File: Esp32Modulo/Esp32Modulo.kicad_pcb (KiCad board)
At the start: 2 copper layers, 50 x 50 mm, 22 parts, among them J4 Alimentacion, U1 ESP32, U2 AMS1117-3.3

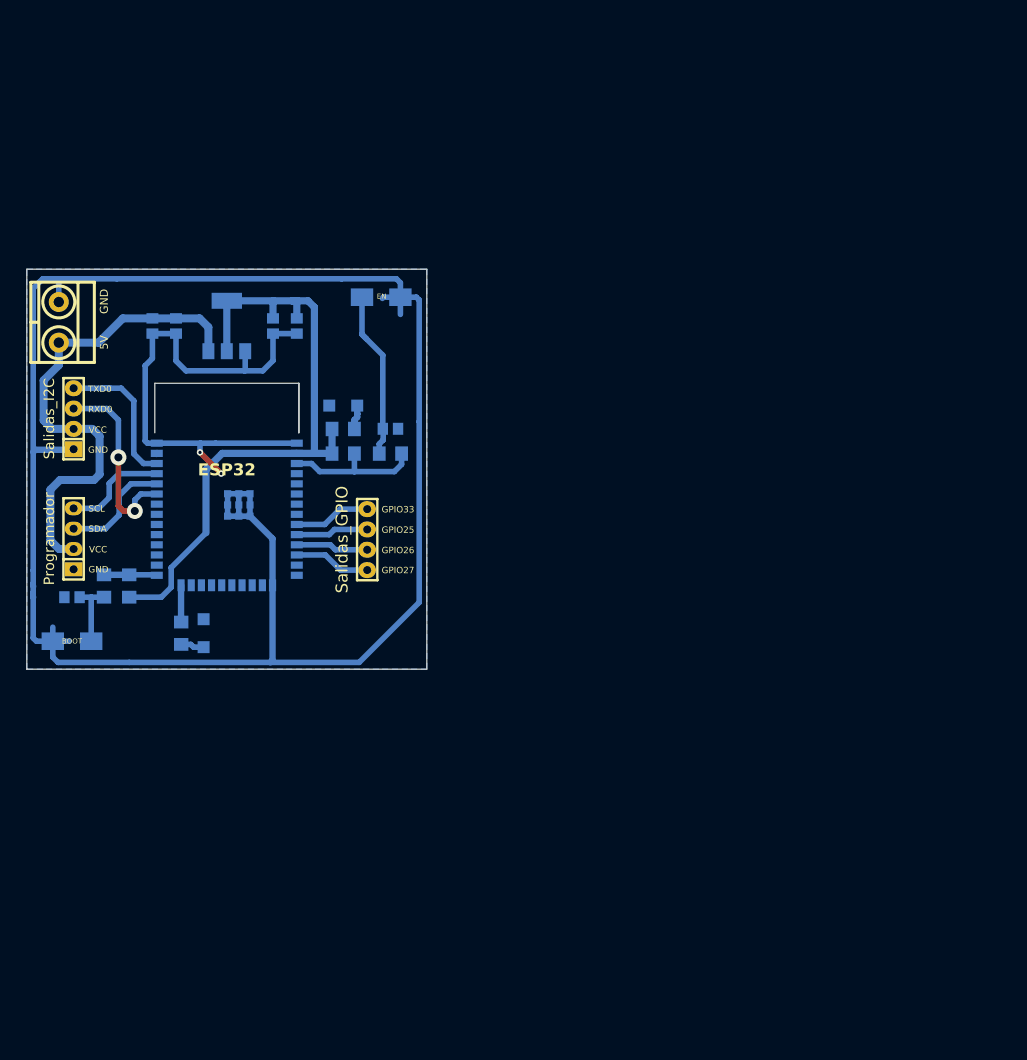
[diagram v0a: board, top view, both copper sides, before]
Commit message: modificaciones al PCB para arreglar el error de pasar pistas por encima de la antena
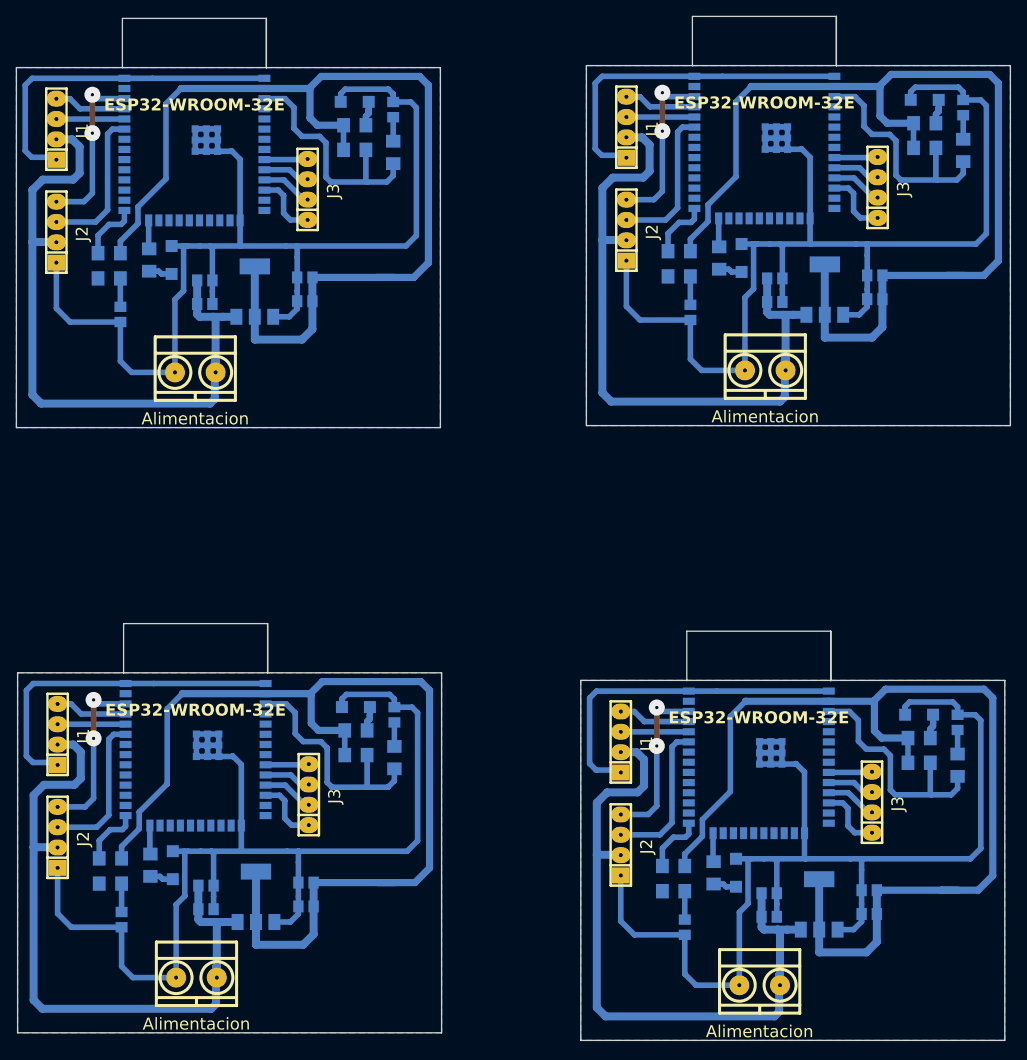
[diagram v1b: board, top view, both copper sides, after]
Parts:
- removed BOOT, EN: SW_Push, footprints:Button
- removed the J4 at (102.2, 71.9)
- removed Programador: Programador, EESTN5:pin_strip_4
- removed Salidas_GPIO: Salidas_GPIO, EESTN5:pin_strip_4
- removed Salidas_I2C: Salidas_I2C(5V), EESTN5:pin_strip_4
- added C1: 10uF, EESTN5:C_0805, B.Cu at (120.6, 145.3)
- added C1: 10uF, EESTN5:C_0805, B.Cu at (191.0, 146.2)
- added C1: 10uF, EESTN5:C_0805, B.Cu at (191.7, 69.4)
- added C2: 100nF, EESTN5:C_0805, B.Cu at (120.6, 142.3)
- added C2: 100nF, EESTN5:C_0805, B.Cu at (191.0, 143.3)
- added C2: 100nF, EESTN5:C_0805, B.Cu at (191.7, 66.5)
- added C3: 10uF, EESTN5:C_0805, B.Cu at (133.2, 142.0)
- added C3: 10uF, EESTN5:C_0805, B.Cu at (204.3, 66.1)
- added C3: 10uF, EESTN5:C_0805, B.Cu at (203.6, 142.9)
- added C4: 100nF, EESTN5:C_0805, B.Cu at (203.6, 145.9)
- added C4: 100nF, EESTN5:C_0805, B.Cu at (204.3, 69.0)
- added C4: 100nF, EESTN5:C_0805, B.Cu at (133.2, 144.9)
- added C5: 1n, EESTN5:C_0805, B.Cu at (181.2, 70.7)
- added C5: 1n, EESTN5:C_0805, B.Cu at (180.5, 147.6)
- added C5: 1n, EESTN5:C_0805, B.Cu at (110.1, 146.6)
- added C6: 1n, EESTN5:C_0805, B.Cu at (215.3, 45.1)
- added C6: 1n, EESTN5:C_0805, B.Cu at (214.6, 122.0)
- added C6: 1n, EESTN5:C_0805, B.Cu at (144.2, 121.0)
- added J1: Programador, EESTN5:pin_strip_4, F.Cu at (102.0, 47.8)
- added J1: Programador, EESTN5:pin_strip_4, F.Cu at (173.2, 47.5)
- added J1: Programador, EESTN5:pin_strip_4, F.Cu at (102.1, 123.5)
- added J1: Programador, EESTN5:pin_strip_4, F.Cu at (172.5, 124.4)
- added J2: Salidas_I2C(5V), EESTN5:pin_strip_4, F.Cu at (102.0, 60.7)
- added J2: Salidas_I2C(5V), EESTN5:pin_strip_4, F.Cu at (102.1, 136.3)
- added J2: Salidas_I2C(5V), EESTN5:pin_strip_4, F.Cu at (172.5, 137.3)
- added J2: Salidas_I2C(5V), EESTN5:pin_strip_4, F.Cu at (173.2, 60.4)
- added J3: Salidas_GPIO, EESTN5:pin_strip_4, F.Cu at (133.5, 131.0)
- added J3: Salidas_GPIO, EESTN5:pin_strip_4, F.Cu at (203.9, 131.9)
- added J3: Salidas_GPIO, EESTN5:pin_strip_4, F.Cu at (204.6, 55.1)
- added J3: Salidas_GPIO, EESTN5:pin_strip_4, F.Cu at (133.3, 55.3)
- added J4: Alimentacion, EESTN5:BORNERA2_AZUL, F.Cu at (189.9, 154.8)
- added J4: Alimentacion, EESTN5:BORNERA2_AZUL, F.Cu at (119.5, 153.8)
- added J4: Alimentacion, EESTN5:BORNERA2_AZUL, F.Cu at (190.6, 78.0)
- added J4: Alimentacion, EESTN5:BORNERA2_AZUL, F.Cu at (119.3, 78.2)
- added LED1: POW, EESTN5:LED_1206, B.Cu at (139.4, 120.0)
- added LED1: POW, EESTN5:LED_1206, B.Cu at (210.5, 44.1)
- added LED1: POW, EESTN5:LED_1206, B.Cu at (209.8, 121.0)
- added LED2: D2, EESTN5:LED_1206, B.Cu at (186.9, 140.7)
- added LED2: D2, EESTN5:LED_1206, B.Cu at (187.6, 63.9)
- added LED2: D2, EESTN5:LED_1206, B.Cu at (116.5, 139.8)
- added R1: 470, EESTN5:R_1206, B.Cu at (108.7, 142.1)
- added R1: 470, EESTN5:R_1206, B.Cu at (179.8, 66.2)
- added R1: 470, EESTN5:R_1206, B.Cu at (179.1, 143.1)
- added R3: 1OK, EESTN5:R_1206, B.Cu at (108.7, 138.9)
- added R3: 1OK, EESTN5:R_1206, B.Cu at (179.8, 63.0)
- added R3: 1OK, EESTN5:R_1206, B.Cu at (179.1, 139.9)
- added R5: 1K, EESTN5:R_1206, B.Cu at (139.4, 123.0)
- added R5: 1K, EESTN5:R_1206, B.Cu at (209.8, 123.9)
- added R5: 1K, EESTN5:R_1206, B.Cu at (210.5, 47.1)
- added R6: 1K, EESTN5:R_1206, B.Cu at (184.8, 63.9)
- added R6: 1K, EESTN5:R_1206, B.Cu at (113.7, 139.8)
- added R6: 1K, EESTN5:R_1206, B.Cu at (184.1, 140.8)
- added R7: 470, EESTN5:R_1206, B.Cu at (214.6, 127.3)
- added R7: 470, EESTN5:R_1206, B.Cu at (215.3, 50.5)
- added R7: 470, EESTN5:R_1206, B.Cu at (144.2, 126.4)
- added R8: 10K, EESTN5:R_1206, B.Cu at (210.5, 50.1)
- added R8: 10K, EESTN5:R_1206, B.Cu at (209.8, 127.0)
- added R8: 10K, EESTN5:R_1206, B.Cu at (139.4, 126.0)
- added U1: ESP32-WROOM-32E, footprints:ESP32-WROOM-32E, B.Cu at (189.8, 126.3)
- added U1: ESP32-WROOM-32E, footprints:ESP32-WROOM-32E, B.Cu at (190.4, 49.4)
- added U1: ESP32-WROOM-32E, footprints:ESP32-WROOM-32E, B.Cu at (119.3, 125.3)
- added U2: AMS1117-3.3, footprints:SOT-223-3_TabPin2, B.Cu at (126.9, 143.8)
- added U2: AMS1117-3.3, footprints:SOT-223-3_TabPin2, B.Cu at (197.3, 144.7)
- added U2: AMS1117-3.3, footprints:SOT-223-3_TabPin2, B.Cu at (198.0, 67.8)
- U1: value ESP32 -> ESP32-WROOM-32E
- moved LED2 46.8 mm to (116.3, 64.1)
- moved R6 46.8 mm to (113.5, 64.2)
- moved U1 45.8 mm to (119.2, 49.7)
- moved R3 41.7 mm to (108.5, 63.3), turned to 180 degrees
- moved C6 39.9 mm to (144.1, 45.4), turned to 90 degrees
- moved R1 38.5 mm to (108.5, 66.5), turned to 0 degrees
- moved R5 38.0 mm to (139.2, 47.3)
- moved LED1 38.0 mm to (139.2, 44.4)
- moved R8 38.0 mm to (139.2, 50.4)
- moved R7 37.6 mm to (144.1, 50.7), turned to 90 degrees
- moved C5 35.9 mm to (110.0, 71.0), turned to -90 degrees
- moved C3 7.26 mm to (133.0, 66.3), turned to 0 degrees
- moved C1 7.10 mm to (120.5, 69.7), turned to 180 degrees
- moved C2 6.74 mm to (120.5, 66.7), turned to 180 degrees
- moved U2 5.54 mm to (126.8, 68.1)
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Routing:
- net GND: track 303.5 -> 778.8 mm, vias 2 -> 0
- net +3V3: track 83.0 -> 520.1 mm
- net +5V: track 63.1 -> 346.3 mm
- net /EN: track 17.5 -> 121.4 mm
- net /SCL: track 19.3 -> 85.8 mm, vias 0 -> 8
- net /SDA: track 23.9 -> 75.5 mm, vias 2 -> 0
- net /IO0: track 6.62 -> 30.4 mm
- net /IO27: track 9.58 -> 33.0 mm
- net /TXD0: track 13.2 -> 36.1 mm
- net /RXD0: track 14.1 -> 34.0 mm
- net /IO26: track 9.06 -> 25.7 mm
- net /IO25: track 9.07 -> 23.6 mm
- net /IO33: track 9.60 -> 21.7 mm
- net Net-(LED1-A): track 3.44 -> 13.7 mm
- net /IO2: track 4.62 -> 14.3 mm
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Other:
- board size 50 x 50 mm -> 124.2 x 121.8 mm
- board text removed: "5V"
- board text removed: "GND"
- board text removed: "GPIO25"
- board text removed: "GPIO26"
- board text removed: "GPIO27"
- board text removed: "GPIO33"
- board text removed: "RXD0"
- board text removed: "SCL"
- board text removed: "SDA"
- board text removed: "TXD0"
- board text removed: "VCC"

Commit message: PCB con el error de la antena corregido y terminado
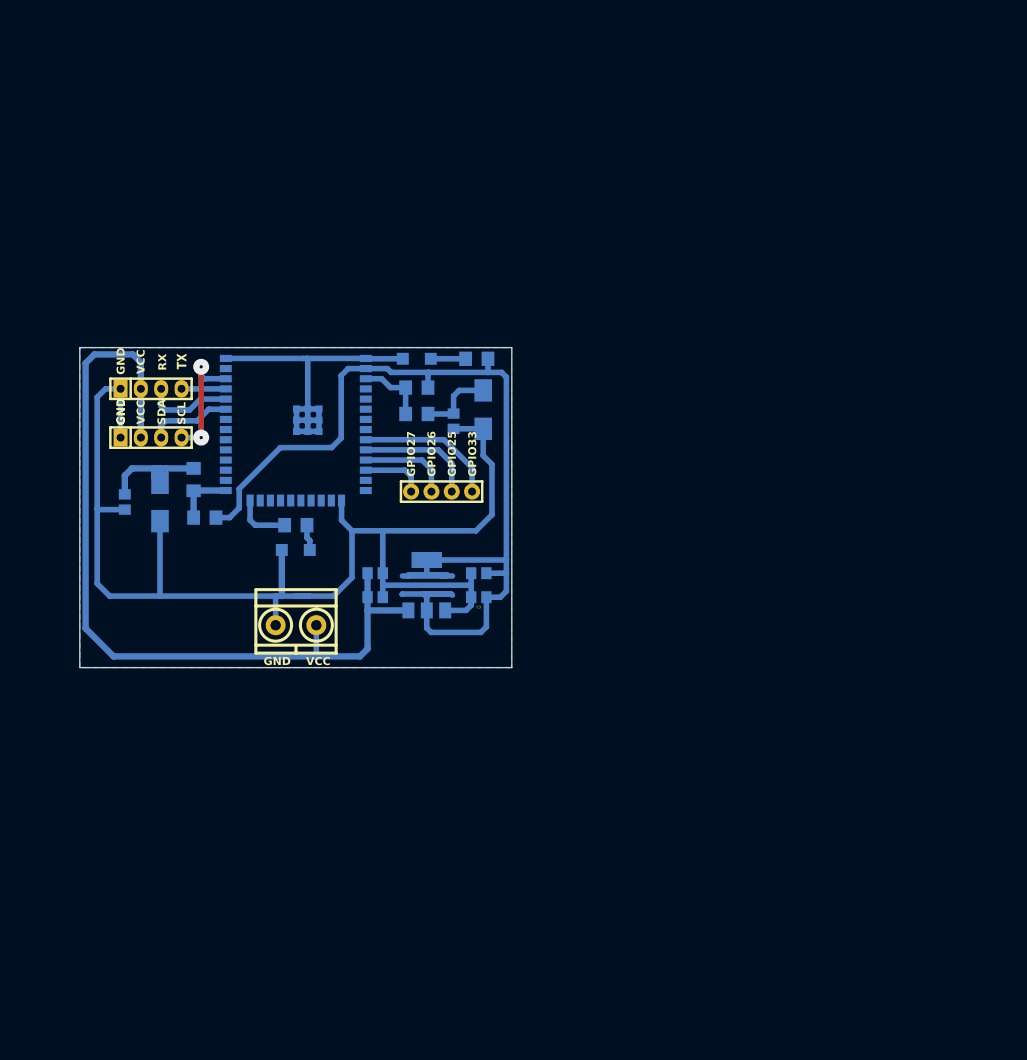
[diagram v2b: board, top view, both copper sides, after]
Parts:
- removed the C1 at (120.6, 145.3)
- removed the C1 at (191.0, 146.2)
- removed the C1 at (191.7, 69.4)
- removed the C1 at (120.5, 69.7)
- removed the C2 at (120.6, 142.3)
- removed the C2 at (191.0, 143.3)
- removed the C2 at (191.7, 66.5)
- removed the C2 at (120.5, 66.7)
- removed the C3 at (133.2, 142.0)
- removed the C3 at (204.3, 66.1)
- removed the C3 at (133.0, 66.3)
- removed the C3 at (203.6, 142.9)
- removed the C4 at (133.0, 69.3)
- removed the C4 at (203.6, 145.9)
- removed the C4 at (204.3, 69.0)
- removed the C4 at (133.2, 144.9)
- removed the C5 at (181.2, 70.7)
- removed the C5 at (180.5, 147.6)
- removed the C5 at (110.0, 71.0)
- removed the C5 at (110.1, 146.6)
- removed the C6 at (215.3, 45.1)
- removed the C6 at (144.1, 45.4)
- removed the C6 at (214.6, 122.0)
- removed the C6 at (144.2, 121.0)
- removed the J1 at (102.0, 47.8)
- removed the J1 at (173.2, 47.5)
- removed the J1 at (102.1, 123.5)
- removed the J1 at (172.5, 124.4)
- removed the J2 at (102.0, 60.7)
- removed the J2 at (102.1, 136.3)
- removed the J2 at (172.5, 137.3)
- removed the J2 at (173.2, 60.4)
- removed the J3 at (133.5, 131.0)
- removed the J3 at (203.9, 131.9)
- removed the J3 at (204.6, 55.1)
- removed the J3 at (133.3, 55.3)
- removed the J4 at (189.9, 154.8)
- removed the J4 at (119.5, 153.8)
- removed the J4 at (190.6, 78.0)
- removed the J4 at (119.3, 78.2)
- removed the LED1 at (139.4, 120.0)
- removed the LED1 at (210.5, 44.1)
- removed the LED1 at (139.2, 44.4)
- removed the LED1 at (209.8, 121.0)
- removed the LED2 at (186.9, 140.7)
- removed the LED2 at (116.3, 64.1)
- removed the LED2 at (187.6, 63.9)
- removed the LED2 at (116.5, 139.8)
- removed the R1 at (108.7, 142.1)
- removed the R1 at (108.5, 66.5)
- removed the R1 at (179.8, 66.2)
- removed the R1 at (179.1, 143.1)
- removed the R3 at (108.7, 138.9)
- removed the R3 at (179.8, 63.0)
- removed the R3 at (108.5, 63.3)
- removed the R3 at (179.1, 139.9)
- removed the R5 at (139.2, 47.3)
- removed the R5 at (139.4, 123.0)
- removed the R5 at (209.8, 123.9)
- removed the R5 at (210.5, 47.1)
- removed the R6 at (113.5, 64.2)
- removed the R6 at (184.8, 63.9)
- removed the R6 at (113.7, 139.8)
- removed the R6 at (184.1, 140.8)
- removed the R7 at (214.6, 127.3)
- removed the R7 at (215.3, 50.5)
- removed the R7 at (144.1, 50.7)
- removed the R7 at (144.2, 126.4)
- removed the R8 at (139.2, 50.4)
- removed the R8 at (210.5, 50.1)
- removed the R8 at (209.8, 127.0)
- removed the R8 at (139.4, 126.0)
- removed the U1 at (189.8, 126.3)
- removed the U1 at (190.4, 49.4)
- removed the U1 at (119.3, 125.3)
- removed the U1 at (119.2, 49.7)
- removed the U2 at (126.8, 68.1)
- removed the U2 at (126.9, 143.8)
- removed the U2 at (197.3, 144.7)
- removed the U2 at (198.0, 67.8)
- added BOOT1: SW_Push, footprints:Button, B.Cu at (114.9, 94.4)
- added C1: 10uF, EESTN5:C_0805, B.Cu at (141.8, 103.3)
- added C2: 100nF, EESTN5:C_0805, B.Cu at (141.8, 106.3)
- added C3: 10uF, EESTN5:C_0805, B.Cu at (154.7, 106.3)
- added C4: 100nF, EESTN5:C_0805, B.Cu at (154.7, 103.3)
- added C5: 1n, EESTN5:C_0805, B.Cu at (110.5, 94.4)
- added C6: 1n, EESTN5:C_0805, B.Cu at (151.6, 84.3)
- added EN1: SW_Push, footprints:Button, B.Cu at (155.3, 82.8)
- added J1: Programador, EESTN5:pin_strip_4, F.Cu at (113.8, 80.2)
- added J2: Salidas_I2C(5V), EESTN5:pin_strip_4, F.Cu at (113.8, 86.3)
- added J3: Salidas_GPIO, EESTN5:pin_strip_4, F.Cu at (150.1, 93.1)
- added J4: Alimentacion, EESTN5:BORNERA2_AZUL, F.Cu at (131.9, 109.8)
- added LED1: POW, EESTN5:LED_1206, B.Cu at (147.0, 76.5)
- added LED2: D2, EESTN5:LED_1206, B.Cu at (131.9, 100.4)
- added R1: 470, EESTN5:R_1206, B.Cu at (119.1, 91.6)
- added R3: 1OK, EESTN5:R_1206, B.Cu at (120.5, 96.3)
- added R5: 1K, EESTN5:R_1206, B.Cu at (154.5, 76.5)
- added R6: 1K, EESTN5:R_1206, B.Cu at (131.9, 97.3)
- added R7: 470, EESTN5:R_1206, B.Cu at (147.0, 83.4)
- added R8: 10K, EESTN5:R_1206, B.Cu at (147.0, 80.1)
- added U1: ESP32-WROOM-32E, footprints:ESP32-WROOM-32E, B.Cu at (131.9, 84.7)
- added U2: AMS1117-3.3, footprints:SOT-223-3_TabPin2, B.Cu at (148.2, 104.8)
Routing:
- net GND: track 778.8 -> 206.0 mm
- net +3V3: track 520.1 -> 135.2 mm
- net +5V: track 346.3 -> 105.9 mm
- net /EN: track 121.4 -> 8.74 mm
- net /SCL: track 85.8 -> 15.7 mm, vias 8 -> 2
- net /SDA: track 75.5 -> 10.5 mm
- net /TXD0: track 36.1 -> 5.54 mm
- net /IO27: track 33.0 -> 7.89 mm
- net /IO0: track 30.4 -> 7.39 mm
- net /RXD0: track 34.0 -> 11.0 mm
- net /IO26: track 25.7 -> 11.5 mm
- net Net-(LED1-A): track 13.7 -> 4.36 mm
- net /IO25: track 23.6 -> 15.0 mm
- net Net-(LED2-A): track 11.8 -> 3.25 mm
- net /IO2: track 14.3 -> 7.03 mm
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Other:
- board size 124.2 x 121.8 mm -> 54 x 40 mm
- board text added: "GND"
- board text added: "GPIO25"
- board text added: "GPIO26"
- board text added: "GPIO27"
- board text added: "GPIO33"
- board text added: "RX"
- board text added: "SCL"
- board text added: "SDA"
- board text added: "TX"
- board text added: "VCC"
